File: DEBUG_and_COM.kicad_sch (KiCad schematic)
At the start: 11 parts, among them J5 COM Port, U4 CH340G, U5 SRV05-4, U6 MAX485E, Y1 12MHz

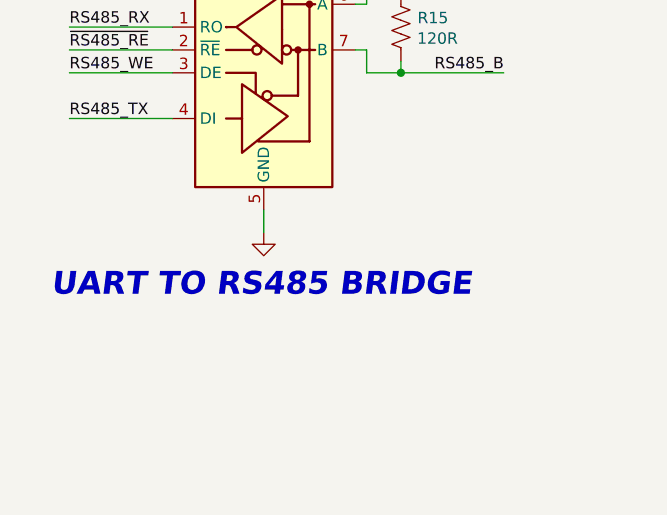
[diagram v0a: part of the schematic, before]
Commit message: Specefies which section is complete and incomplete
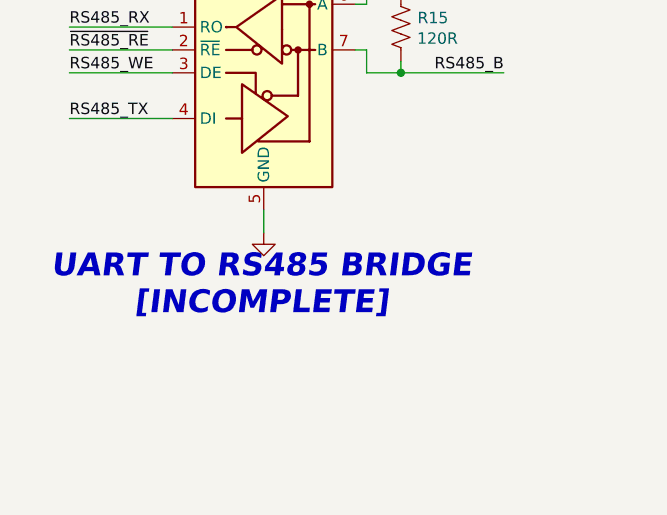
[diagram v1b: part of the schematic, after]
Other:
- note added: "UART TO RS485 BRIDGE [INCOMPLETE]"
- note removed: "UART TO RS485 BRIDGE"
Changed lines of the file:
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@@
 		)
 	)
-	(text "UART TO RS485 BRIDGE"
+	(text "UART TO RS485 BRIDGE\n[INCOMPLETE]"
 		(exclude_from_sim no)
 		(at 96.266 107.442 0)

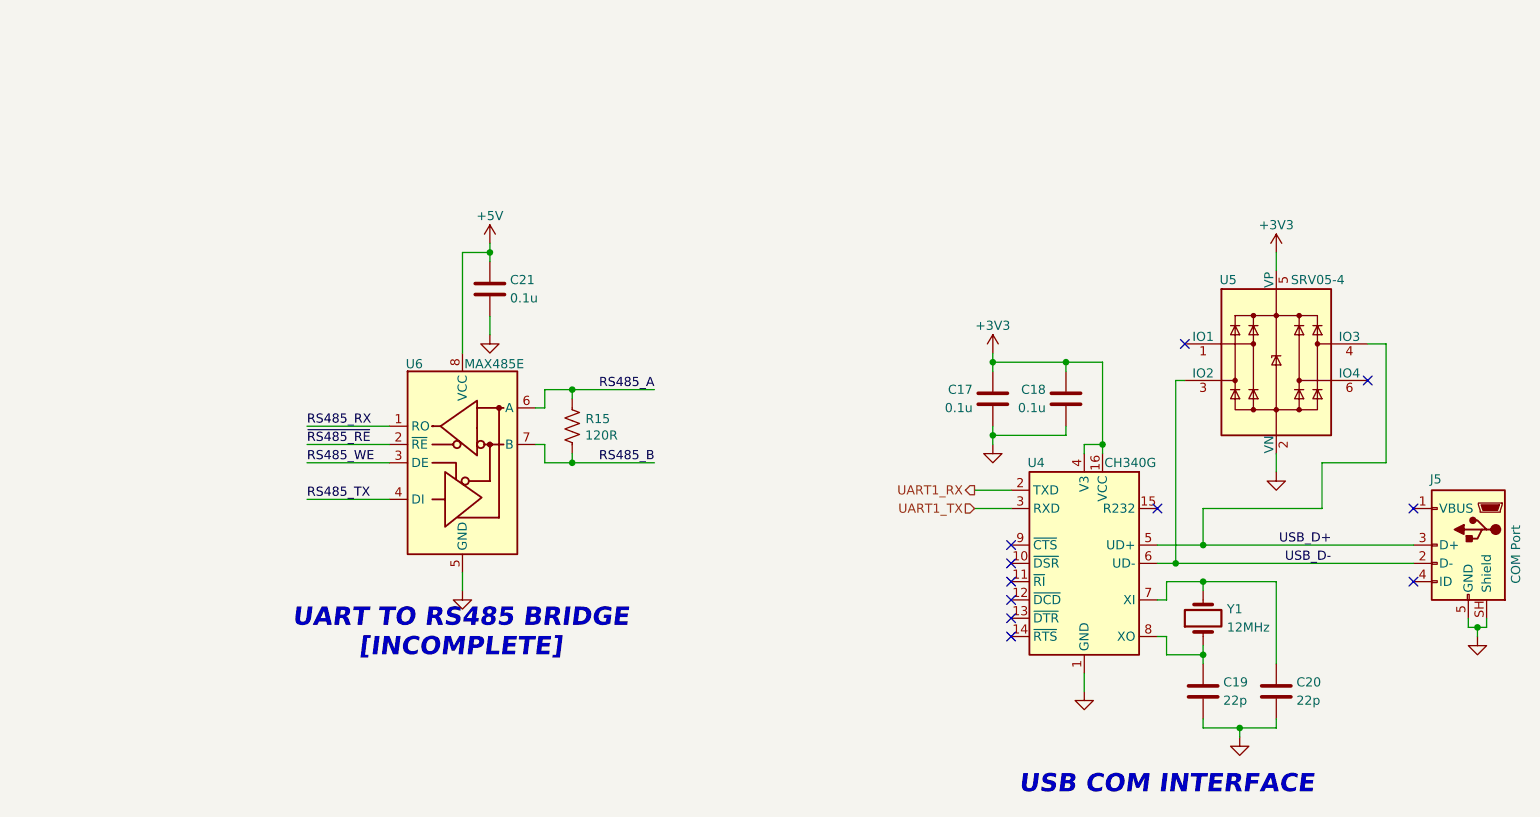
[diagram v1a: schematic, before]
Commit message: Optocoupler added for RS485 communication (DEBUG_and_COM)
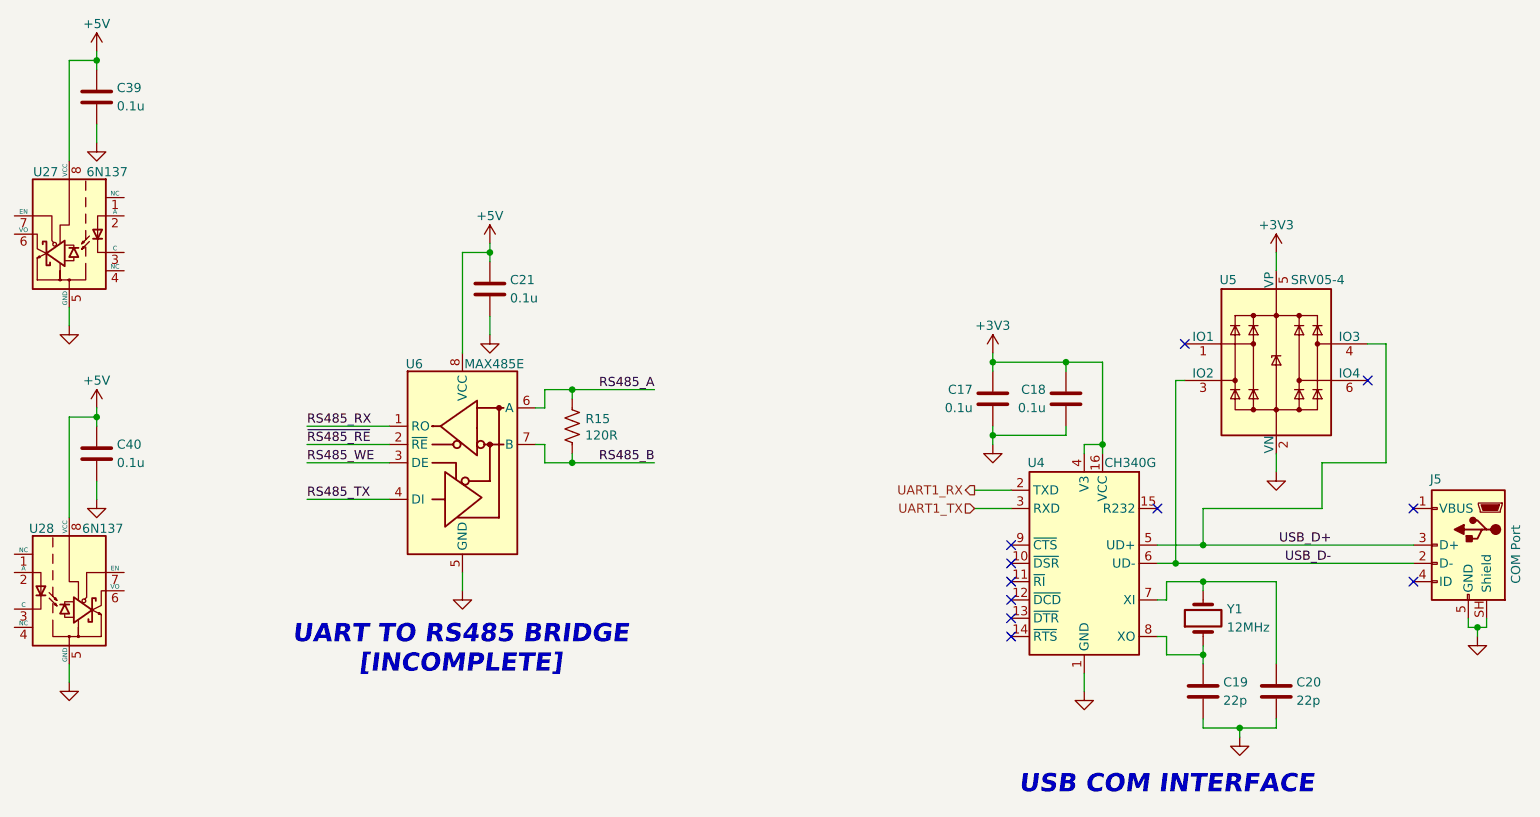
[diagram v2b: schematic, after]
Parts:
- added C39, C40: 0.1u, Capacitor_SMD:C_0603_1608Metric_Pad1.08x0.95mm_HandSolder, symbol Device:C
- added U27, U28: 6N137, Package_DIP:DIP-8_W7.62mm, symbol Isolator:6N137
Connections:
- net +5V: now also C39.1, C40.1, U27.8 (VCC), U28.8 (VCC)
- net GND: now also C39.2, C40.2, U27.5 (GND), U28.5 (GND)
